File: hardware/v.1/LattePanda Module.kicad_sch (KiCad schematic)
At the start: 12 parts, among them J1 Conn_01x03_Pin

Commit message: finish the back IO, roughly establish HSIO placement
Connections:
- net USB_2_P1+: now also A1.75 (USB2_P2+); no longer A1.69 (USB2_P1+)
- net USB_2_P1-: now also A1.73 (USB2_P2-); no longer A1.67 (USB2_P1-)
- net USB_2_P2+: now also A1.69 (USB2_P1+); no longer A1.75 (USB2_P2+)
- net USB_2_P2-: now also A1.67 (USB2_P1-); no longer A1.73 (USB2_P2-)
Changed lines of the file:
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@@
+		)
+	)
+	(hierarchical_label "USB_2_P2-"
+		(shape bidirectional)
+		(at 238.76 177.8 180)
+		(effects
+			(font
+				(size 1.27 1.27)
+			)
+			(justify right)
+		)
+	)
+	(hierarchical_label "~{PEWAKE}"
+		(shape output)
+		(at 369.57 76.2 0)
+		(effects
+			(font
+				(size 1.27 1.27)
+			)
+			(justify left)
 		)
 	)
 	(hierarchical_label "USB_2_P1-"
 		(shape bidirectional)
-		(at 238.76 177.8 180)
-		(effects
-			(font
-				(size 1.27 1.27)
-			)
-			(justify right)
-		)
-	)
-	(hierarchical_label "~{PEWAKE}"
-		(shape output)
-		(at 369.57 76.2 0)
-		(effects
-			(font
-				(size 1.27 1.27)
-			)
-			(justify left)
-		)
-	)
-	(hierarchical_label "USB_2_P2-"
-		(shape bidirectional)
 		(at 238.76 182.88 180)
 		(effects
@@
 		)
 	)
+	(hierarchical_label "USB_2_P1+"
+		(shape bidirectional)
+		(at 238.76 180.34 180)
+		(effects
+			(font
+				(size 1.27 1.27)
+			)
+			(justify right)
+		)
+	)
+	(hierarchical_label "HSIO_1_RX+"
+		(shape input)
+		(at 238.76 93.98 180)
+		(effects
+			(font
+				(size 1.27 1.27)
+			)
+			(justify right)
+		)
+	)
+	(hierarchical_label "SOC_UART2_TX"
+		(shape output)
+		(at 368.3 190.5 0)
+		(effects
+			(font
+				(size 1.27 1.27)
+			)
+			(justify left)
+		)
+	)
+	(hierarchical_label "HSIO_2_RX+"
+		(shape input)
+		(at 238.76 104.14 180)
+		(effects
+			(font
+				(size 1.27 1.27)
+			)
+			(justify right)
+		)
+	)
+	(hierarchical_label "DDI_B_TX1-"
+		(shape output)
+		(at 238.76 236.22 180)
+		(effects
+			(font
+				(size 1.27 1.27)
+			)
+			(justify right)
+		)
+	)
+	(hierarchical_label "HSIO_9_RX-"
+		(shape input)
+		(at 238.76 139.7 180)
+		(effects
+			(font
+				(size 1.27 1.27)
+			)
+			(justify right)
+		)
+	)
+	(hierarchical_label "HSIO_10_RX+"
+		(shape input)
+		(at 238.76 147.32 180)
+		(effects
+			(font
+				(size 1.27 1.27)
+			)
+			(justify right)
+		)
+	)
+	(hierarchical_label "HSIO_10_TX-"
+		(shape output)
+		(at 238.76 144.78 180)
+		(effects
+			(font
+				(size 1.27 1.27)
+			)
+			(justify right)
+		)
+	)
+	(hierarchical_label "USB_2_P5-"
+		(shape bidirectional)
+		(at 369.57 119.38 0)
+		(effects
+			(font
+				(size 1.27 1.27)
+			)
+			(justify left)
+		)
+	)
+	(hierarchical_label "REFCLK4+"
+		(shape output)
+		(at 369.57 102.87 0)
+		(effects
+			(font
+				(size 1.27 1.27)
+			)
+			(justify left)
+		)
+	)
+	(hierarchical_label "~{PLT_RST}"
+		(shape output)
+		(at 369.57 78.74 0)
+		(effects
+			(font
+				(size 1.27 1.27)
+			)
+			(justify left)
+		)
+	)
+	(hierarchical_label "HSIO_0_RX-"
+		(shape input)
+		(at 238.76 86.36 180)
+		(effects
+			(font
+				(size 1.27 1.27)
+			)
+			(justify right)
+		)
+	)
 	(hierarchical_label "USB_2_P2+"
 		(shape bidirectional)
-		(at 238.76 180.34 180)
-		(effects
-			(font
-				(size 1.27 1.27)
-			)
-			(justify right)
-		)
-	)
-	(hierarchical_label "HSIO_1_RX+"
-		(shape input)
-		(at 238.76 93.98 180)
-		(effects
-			(font
-				(size 1.27 1.27)
-			)
-			(justify right)
-		)
-	)
-	(hierarchical_label "SOC_UART2_TX"
-		(shape output)
-		(at 368.3 190.5 0)
-		(effects
-			(font
-				(size 1.27 1.27)
-			)
-			(justify left)
-		)
-	)
-	(hierarchical_label "HSIO_2_RX+"
-		(shape input)
-		(at 238.76 104.14 180)
-		(effects
-			(font
-				(size 1.27 1.27)
-			)
-			(justify right)
-		)
-	)
-	(hierarchical_label "DDI_B_TX1-"
-		(shape output)
-		(at 238.76 236.22 180)
-		(effects
-			(font
-				(size 1.27 1.27)
-			)
-			(justify right)
-		)
-	)
-	(hierarchical_label "HSIO_9_RX-"
-		(shape input)
-		(at 238.76 139.7 180)
-		(effects
-			(font
-				(size 1.27 1.27)
-			)
-			(justify right)
-		)
-	)
-	(hierarchical_label "HSIO_10_RX+"
-		(shape input)
-		(at 238.76 147.32 180)
-		(effects
-			(font
-				(size 1.27 1.27)
-			)
-			(justify right)
-		)
-	)
-	(hierarchical_label "HSIO_10_TX-"
-		(shape output)
-		(at 238.76 144.78 180)
-		(effects
-			(font
-				(size 1.27 1.27)
-			)
-			(justify right)
-		)
-	)
-	(hierarchical_label "USB_2_P5-"
-		(shape bidirectional)
-		(at 369.57 119.38 0)
-		(effects
-			(font
-				(size 1.27 1.27)
-			)
-			(justify left)
-		)
-	)
-	(hierarchical_label "REFCLK4+"
-		(shape output)
-		(at 369.57 102.87 0)
-		(effects
-			(font
-				(size 1.27 1.27)
-			)
-			(justify left)
-		)
-	)
-	(hierarchical_label "~{PLT_RST}"
-		(shape output)
-		(at 369.57 78.74 0)
-		(effects
-			(font
-				(size 1.27 1.27)
-			)
-			(justify left)
-		)
-	)
-	(hierarchical_label "HSIO_0_RX-"
-		(shape input)
-		(at 238.76 86.36 180)
-		(effects
-			(font
-				(size 1.27 1.27)
-			)
-			(justify right)
-		)
-	)
-	(hierarchical_label "USB_2_P1+"
-		(shape bidirectional)
 		(at 238.76 175.26 180)

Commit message: wire up the 3 pcie lanes coming from the realtek ic and add 2 usbc ports
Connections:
- net HSIO_6_TX+: now also A1.63 (HSIO6_TX-); no longer A1.61 (HSIO6_TX+)
- net HSIO_6_TX-: now also A1.61 (HSIO6_TX+); no longer A1.63 (HSIO6_TX-)
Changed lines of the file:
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@@
 		)
 	)
-	(hierarchical_label "HSIO_6_TX-"
+	(hierarchical_label "HSIO_6_TX+"
 		(shape output)
 		(at 238.76 167.64 180)
@@
 		)
 	)
-	(hierarchical_label "HSIO_6_TX+"
+	(hierarchical_label "HSIO_6_TX-"
 		(shape output)
 		(at 238.76 165.1 180)

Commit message: pretty much finish the board, did bios chip, gpio, 4x sata
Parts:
- added J88: Conn_01x03_Pin, Connector_PinHeader_2.54mm:PinHeader_1x03_P2.54mm_Vertical, symbol Connector:Conn_01x03_Pin
- added R95: 10K/1%, A_HDJ_Library:R_0402_1005Metric, symbol Device:R
- R2: LCSC Part # (none) -> C60490; MPN (none) -> RC0402FR-0710KL; Package (none) -> 0402; Part# (none) -> C60490
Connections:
- net GND: now also R95.1
- net at A1.133 (~{BIOS_SEL}), TP7.1: now also J88.2 (Pin_2); no longer R2.1
- net SPI_IO3: now reaches A1.153 (SPI_IO3)
- net SPI_CLK: now reaches A1.155 (SPI_CLK)
- net SPI_IO0: now reaches A1.159 (SPI_MOSI/SPI_IO0)
- net SPI_IO2: now reaches A1.161 (SPI_IO2)
- net SPI_IO1: now reaches A1.163 (SPI_MISO/SPI_IO1)
- net SPI_CS: now reaches A1.165 (~{SPI_CS})
- net USB_2_P4+: now reaches A1.70 (USB2_P4+)
- net USB_2_P4-: now reaches A1.72 (USB2_P4-)
- net USB_2_P8+: now reaches A1.82 (USB2_P8+)
- net USB_2_P8-: now reaches A1.84 (USB2_P8-)
- new net: J88.1 (Pin_1), R95.2
- new net: J88.3 (Pin_3), R2.1
- no-connect marks 88 -> 78
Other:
- note added: "Cuprum has a second BIOS ROM ~{BIOS_SEL} pull up to 3.3V to select ROM on LattePanda Mu"
- note removed: "Lite Carrier has no second BIOS ROM ~{BIOS_SEL} pull up to 3.3V to select ROM on LattePanda Mu"
- moved on the sheet: R2

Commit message: fix power supply lines
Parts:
- added TP81, TP82, TP83, TP84: TestPoint, A_HDJ_Library:TestPoint_Pad_D1.5mm, symbol Connector:TestPoint
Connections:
- net SOC_UART0_RX: no longer names the net of A1.137 (UART0_RXD)
- net SOC_UART0_RX: now also TP81.1
- net SOC_UART0_TX: no longer names the net of A1.139 (UART0_TXD)
- net SOC_UART0_TX: now also TP82.1
- net SOC_UART1_RX: no longer names the net of A1.141 (UART1_RXD)
- net SOC_UART1_RX: now also TP83.1
- net SOC_UART1_TX: no longer names the net of A1.143 (UART1_TXD)
- net SOC_UART1_TX: now also TP84.1

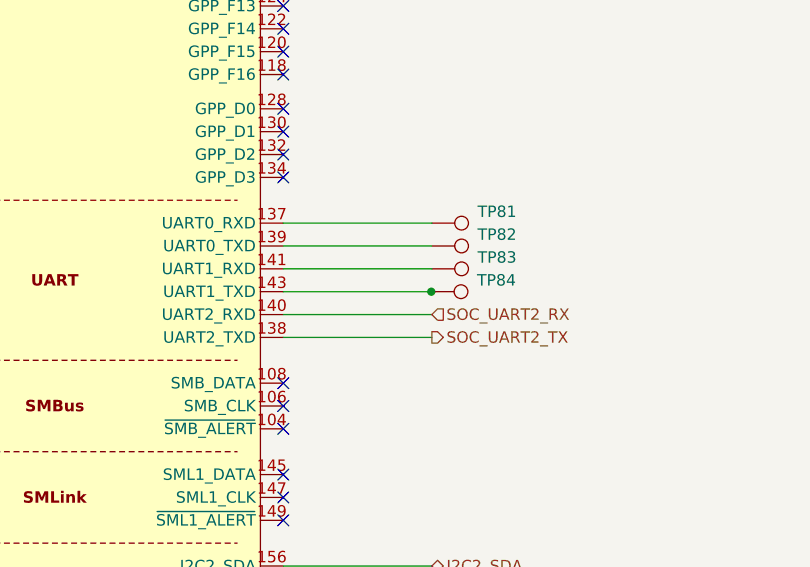
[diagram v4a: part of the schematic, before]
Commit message: design review finished: 0.4/0.2 vias changed to 0.4/0.3, VDC polygon and associated reroute, SATA connector, more ground vias, UART testpoints added, fixed unconnects; DRC at minimum. The BIOS sheet is faulty here (causing all remaining DRC errors)
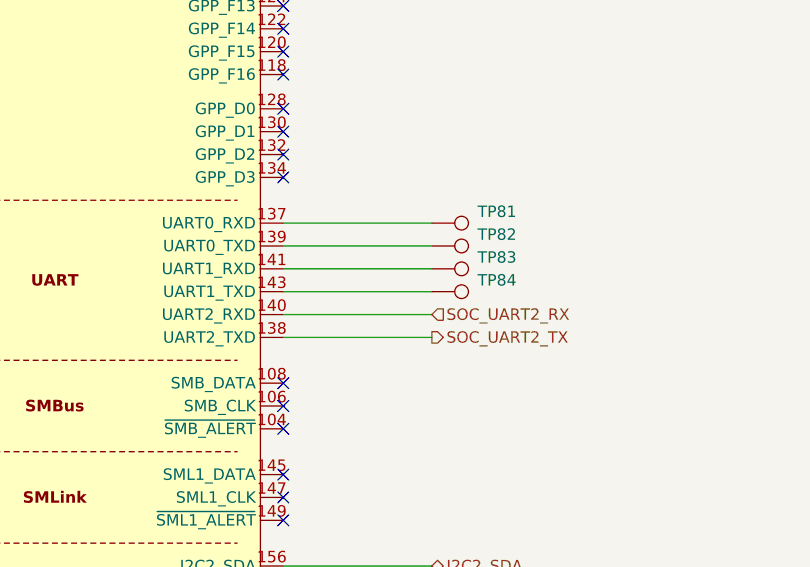
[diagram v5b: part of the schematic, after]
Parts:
- TP81, TP82, TP83, TP84: footprint A_HDJ_Library:TestPoint_Pad_D1.5mm -> A_HDJ_Library:TestPoint_Pad_D1.0mm
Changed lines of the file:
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@@
 	)
 	(junction
-		(at 368.2348 185.42)
-		(diameter 0)
-		(color 0 0 0 0)
-	)
-	(junction
 		(at 355.6 256.54)
 		(diameter 0)
@@
 	(wire
 		(pts
-			(xy 368.2348 185.42) (xy 368.3 185.42)
-		)
-		(stroke
-			(width 0)
-			(type default)
-		)
-	)
-	(wire
-		(pts
 			(xy 309.88 44.45) (xy 309.88 55.88)
 		)
@@
 	(wire
 		(pts
-			(xy 351.79 185.42) (xy 368.2348 185.42)
+			(xy 351.79 185.42) (xy 368.3 185.42)
 		)
 		(stroke
@@
 			)
 		)
-		(property "Footprint" "A_HDJ_Library:TestPoint_Pad_D1.5mm"
+		(property "Footprint" "A_HDJ_Library:TestPoint_Pad_D1.0mm"
 			(at 368.3 185.42 0)
 			(effects
@@
 			)
 		)
-		(property "Footprint" "A_HDJ_Library:TestPoint_Pad_D1.5mm"
+		(property "Footprint" "A_HDJ_Library:TestPoint_Pad_D1.0mm"
 			(at 368.3 182.88 0)
 			(effects
@@
 			)
 		)
-		(property "Footprint" "A_HDJ_Library:TestPoint_Pad_D1.5mm"
+		(property "Footprint" "A_HDJ_Library:TestPoint_Pad_D1.0mm"
 			(at 368.3 187.96 0)
 			(effects
@@
 	(symbol
 		(lib_id "Connector:TestPoint")
-		(at 368.2348 185.42 270)
+		(at 368.3 185.42 270)
 		(unit 1)
 		(exclude_from_sim no)
@@
 		(fields_autoplaced yes)
 		(property "Reference" "TP84"
-			(at 373.3148 184.1499 90)
+			(at 373.38 184.1499 90)
 			(effects
 				(font
@@
 		)
 		(property "Value" "TestPoint"
-			(at 373.3148 186.6899 90)
+			(at 373.38 186.6899 90)
 			(effects
 				(font
@@
 			)
 		)
-		(property "Footprint" "A_HDJ_Library:TestPoint_Pad_D1.5mm"
-			(at 368.2348 190.5 0)
+		(property "Footprint" "A_HDJ_Library:TestPoint_Pad_D1.0mm"
+			(at 368.3 190.5 0)
 			(effects
 				(font
@@
 		)
 		(property "Datasheet" "~"
-			(at 368.2348 190.5 0)
+			(at 368.3 190.5 0)
 			(effects
 				(font
@@
 		)
 		(property "Description" "test point"
-			(at 368.2348 185.42 0)
+			(at 368.3 185.42 0)
 			(effects
 				(font
@@
 		)
 		(property "Sim.Device" ""
-			(at 368.2348 185.42 0)
+			(at 368.3 185.42 0)
 			(effects
 				(font
@@
 		)
 		(property "Sim.Pins" ""
-			(at 368.2348 185.42 0)
+			(at 368.3 185.42 0)
 			(effects
 				(font
@@
 		)
 		(property "Sim.Type" ""
-			(at 368.2348 185.42 0)
+			(at 368.3 185.42 0)
 			(effects
 				(font

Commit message: add cad models for components, silkscreen labeling, fix asm1061 ground pour
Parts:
- H5: footprint A_HDJ_Library:MountingHole_3mm_M2_Pad_TopOnly -> MountingHole:MountingHole_2.2mm_M2_DIN965_Pad
- H6: footprint A_HDJ_Library:MountingHole_3mm_M2_Pad_TopOnly -> MountingHole_2.2mm_M2_DIN965_Pad
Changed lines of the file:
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@@
 			)
 		)
-		(property "Footprint" "A_HDJ_Library:MountingHole_3mm_M2_Pad_TopOnly"
+		(property "Footprint" "MountingHole:MountingHole_2.2mm_M2_DIN965_Pad"
 			(at 414.02 299.72 0)
 			(effects
@@
 			)
 		)
-		(property "Footprint" "A_HDJ_Library:MountingHole_3mm_M2_Pad_TopOnly"
+		(property "Footprint" "MountingHole_2.2mm_M2_DIN965_Pad"
 			(at 439.42 299.72 0)
 			(effects

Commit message: remove some footprints to use digikey ones
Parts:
- H6: footprint MountingHole_2.2mm_M2_DIN965_Pad -> MountingHole:MountingHole_2.2mm_M2_DIN965_Pad
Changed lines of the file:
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@@
 			)
 		)
-		(property "Footprint" "MountingHole_2.2mm_M2_DIN965_Pad"
+		(property "Footprint" "MountingHole:MountingHole_2.2mm_M2_DIN965_Pad"
 			(at 439.42 299.72 0)
 			(effects
